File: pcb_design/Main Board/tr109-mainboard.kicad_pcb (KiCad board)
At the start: 2 copper layers, 60.3 x 60.4 mm, 30 parts, among them J1 Raspberry Pi Zero W, J2 ST7735_Screen, J3 Conn_01x04_Female, J4 Conn_01x09_Female, J5 Conn_01x03_Female, J6 Conn_01x02_Female, J6 Conn_01x02_Female-Connector, J7 Conn_01x03_Female, Q1 2N2222A, U1 CAP1206-x-SL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

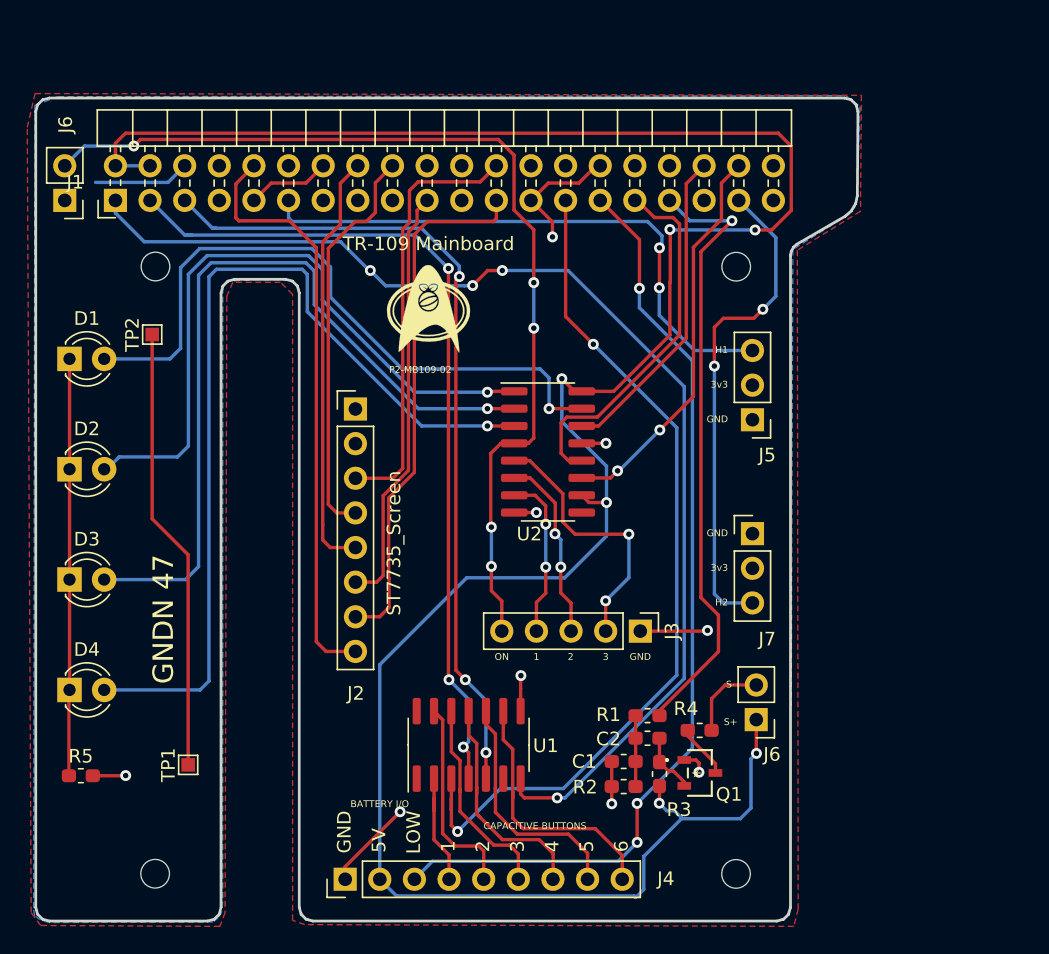
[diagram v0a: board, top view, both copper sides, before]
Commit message: cleanup and revisions
changes to the sensor and main boards
clean up of the blender file to remove some deprecated meshes
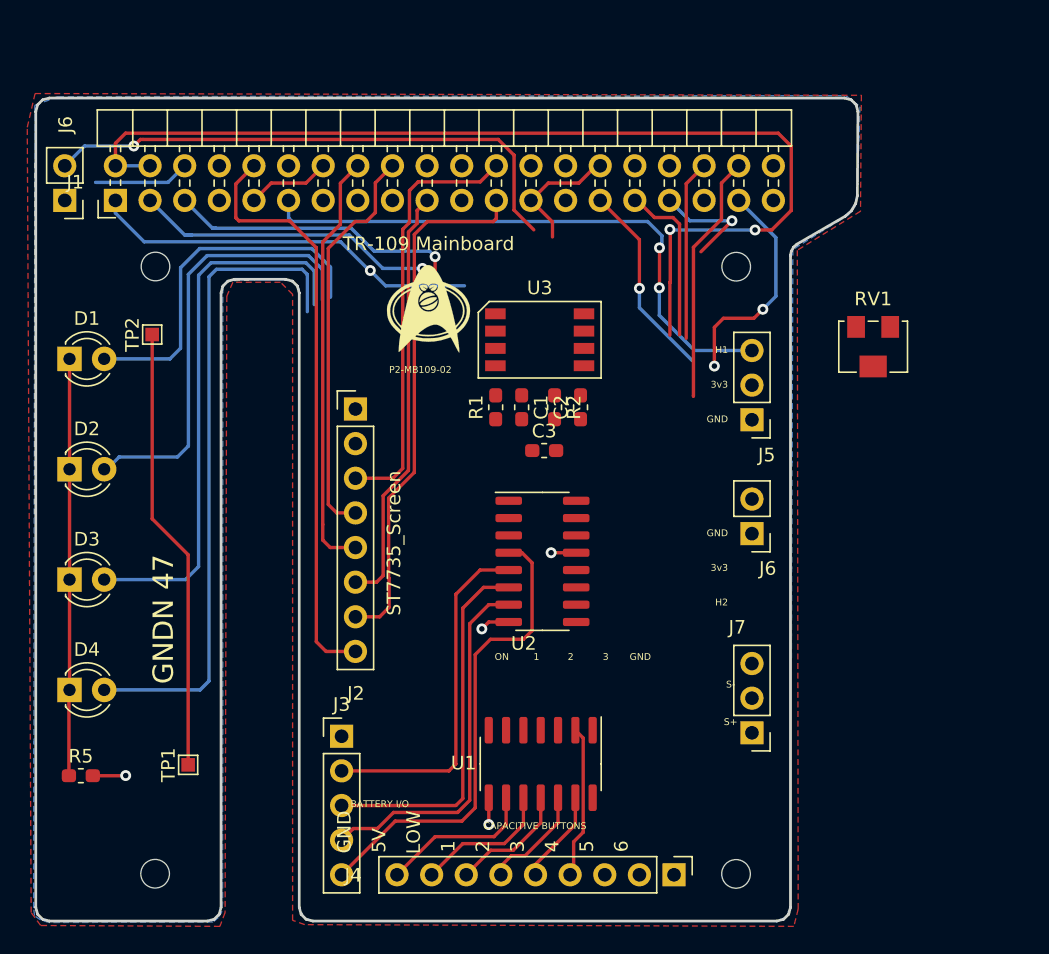
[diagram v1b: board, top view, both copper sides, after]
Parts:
- removed Q1: 2N2222A, footprints:SSTA06HZGT116
- removed R3: 15k, Resistor_SMD:R_0603_1608Metric_Pad1.05x0.95mm_HandSolder
- removed R4: 8, Resistor_SMD:R_0603_1608Metric_Pad1.05x0.95mm_HandSolder
- added C3: 10uF, Capacitor_SMD:C_0603_1608Metric_Pad1.05x0.95mm_HandSolder, F.Cu at (150.9, 96.9)
- added RV1: 10K, Potentiometer_SMD:Potentiometer_Bourns_3214W_Vertical, F.Cu at (175.0, 89.3)
- added U3: PAM8302AAS, Main Board:SOIC-8, F.Cu at (150.5, 88.8)
- C1: value C -> 1uF
- C2: value CP -> 1uF
- R1: value 270 -> 100
- R2: value 150 -> 100
- moved R2 28.3 mm to (151.6, 93.8), turned to 270 degrees
- moved C1 27.0 mm to (149.2, 93.8), turned to 270 degrees
- moved R1 25.2 mm to (147.3, 93.8), turned to 90 degrees
- moved C2 24.8 mm to (153.5, 93.8), turned to 90 degrees
- moved J4 24.1 mm to (160.4, 128.0), turned to 270 degrees
- moved J3 23.2 mm to (136.0, 117.9), turned to 0 degrees
- moved J7 14.6 mm to (166.1, 117.6), turned to 180 degrees
- moved J6 13.6 mm to (166.1, 103.0)
- moved U2 8.04 mm to (150.7, 105.1)
- moved U1 5.47 mm to (150.6, 119.9), turned to 270 degrees
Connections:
- C1 pad 2: GND -> Net-(C1-Pad2)
- C2 pad 1: Net-(C1-Pad1) -> Net-(C2-Pad1)
- C2 pad 2: Net-(C2-Pad2) -> GND
- R1 pad 1: AUDIO -> Net-(R1-Pad1)
- R2 pad 1: GND -> Net-(R2-Pad1)
- R2 pad 2: Net-(C1-Pad1) -> Net-(C2-Pad1)
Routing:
- net 5V: track 179.7 -> 76.5 mm, vias 6 -> 2
- net ALERT: track 63.9 -> 0.00 mm, vias 2 -> 0
- net 3v3: track 87.2 -> 28.7 mm, vias 4 -> 1
- net Bat_GPIO: track 69.0 -> 14.6 mm, vias 3 -> 1
- net SDA: track 62.9 -> 22.5 mm, vias 3 -> 1
- net SCL: track 60.9 -> 22.1 mm, vias 3 -> 1
- net AUDIO: track 44.8 -> 8.41 mm
- net LED1: track 49.1 -> 26.0 mm, vias 1 -> 0
- net Hall_Effect_Sensor2: track 36.2 -> 16.5 mm
- net LED4: track 66.6 -> 47.9 mm, vias 1 -> 0
- net LED3: track 58.1 -> 40.3 mm, vias 1 -> 0
- net LED2: track 49.2 -> 32.3 mm, vias 1 -> 0
- net GND: track 47.8 -> 31.0 mm, vias 9 -> 4
- net Shift_Latch: track 27.5 -> 12.1 mm
- net LED7: track 12.1 -> 27.0 mm, vias 2 -> 0
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
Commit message: Pcb and shell design work
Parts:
- removed G***: LOGO, logo2:smalldelta
- removed G***: LOGO, logo2:delta 3
- removed the J6 at (166.1, 103.0)
- removed the J6 at (115.7, 78.6)
- added J6: Conn_01x02_Female-Connector, Connector_PinHeader_2.54mm:PinHeader_1x02_P2.54mm_Vertical, F.Cu at (164.9, 103.0)
- J4: footprint Connector_PinHeader_2.54mm:PinHeader_1x09_P2.54mm_Vertical -> Connector_PinHeader_2.54mm:PinHeader_1x11_P2.54mm_Vertical
- U1: value CAP1206-x-SL -> CAP1208
- moved J7 43.6 mm to (122.9, 123.5), turned to 270 degrees
- moved J3 29.4 mm to (164.9, 112.0)
- moved RV1 26.0 mm to (150.5, 98.1)
- moved U2 15.2 mm to (150.6, 89.8)
- moved R1 15.2 mm to (146.5, 108.9), turned to 270 degrees
- moved C2 15.2 mm to (154.1, 108.9)
- moved C3 15.1 mm to (150.6, 112.1)
- moved U3 15.1 mm to (150.3, 103.9), turned to 90 degrees
- moved C1 15.1 mm to (149.0, 108.9), turned to 90 degrees
- moved R2 15.1 mm to (151.6, 108.9)
- moved R5 1.73 mm to (116.9, 119.0)
- moved J5 1.24 mm to (164.9, 94.7)
- moved J4 0.48 mm to (160.7, 128.4)
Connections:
- net Net-(J1-Pad35) renamed Shift_Serial_Sensor_Board
- net Net-(J1-Pad40) renamed Shift_Latch_Sensor_Board
- J1 pad 11: Hall_Effect_Sensor -> Net-(J1-Pad11)
- J1 pad 32: Net-(J1-Pad32) -> Hall_Effect_Sensor
- J1 pad 37: Hall_Effect_Sensor2 -> Shift_Clock_Sensor_Board
- J1 pad 7: Net-(J1-Pad7) -> Hall_Effect_Sensor2
- U1 pad 1: (no net) -> Cap_2
- U1 pad 10: Cap_5 -> Cap_7
- U1 pad 11: Cap_4 -> Cap_6
- U1 pad 12: Cap_3 -> Cap_5
- U1 pad 13: Cap_2 -> Cap_4
- U1 pad 14: (no net) -> Cap_3
- U1 pad 9: Cap_6 -> Cap_8
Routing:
- net 5V: track 76.5 -> 183.3 mm, vias 2 -> 8
- net 3v3: track 28.7 -> 98.5 mm, vias 1 -> 7
- net SDA: track 22.5 -> 72.9 mm, vias 1 -> 3
- net ALERT: track 0.00 -> 47.0 mm, vias 0 -> 4
- net SCL: track 22.1 -> 67.2 mm, vias 1 -> 3
- net Bat_GPIO: track 14.6 -> 51.9 mm, vias 1 -> 0
- net Hall_Effect_Sensor2: track 16.5 -> 52.2 mm, vias 2 -> 0
- net LED5: track 25.6 -> 53.4 mm, vias 0 -> 4
- net LED7: track 27.0 -> 53.3 mm, vias 0 -> 4
- net LED6: track 27.1 -> 53.2 mm, vias 0 -> 3
- net Hall_Effect_Sensor: track 43.0 -> 20.1 mm, vias 2 -> 1
- net Net-(J6-Pad2): track 0.00 -> 22.2 mm, vias 0 -> 1
- net LED1: track 26.0 -> 45.2 mm, vias 0 -> 1
- net LED4: track 47.9 -> 67.0 mm, vias 0 -> 1
- net Net-(J6-Pad1): track 0.00 -> 18.2 mm, vias 0 -> 1
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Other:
- board text added: "7"
- board text added: "8"
- board text added: "P2-MB109-03"
- board text removed: "P2-MB109-02"

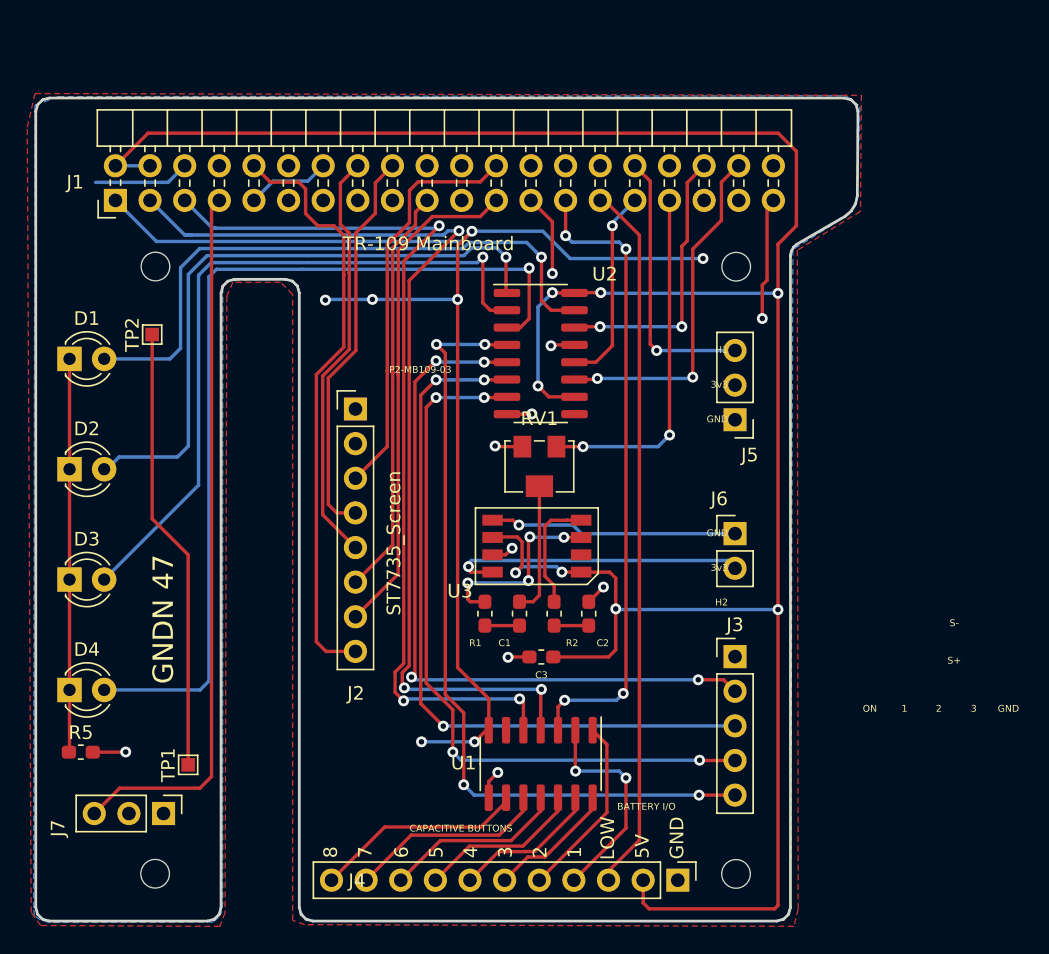
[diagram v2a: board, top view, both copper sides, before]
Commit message: Rev 3 board changes, blender file changes
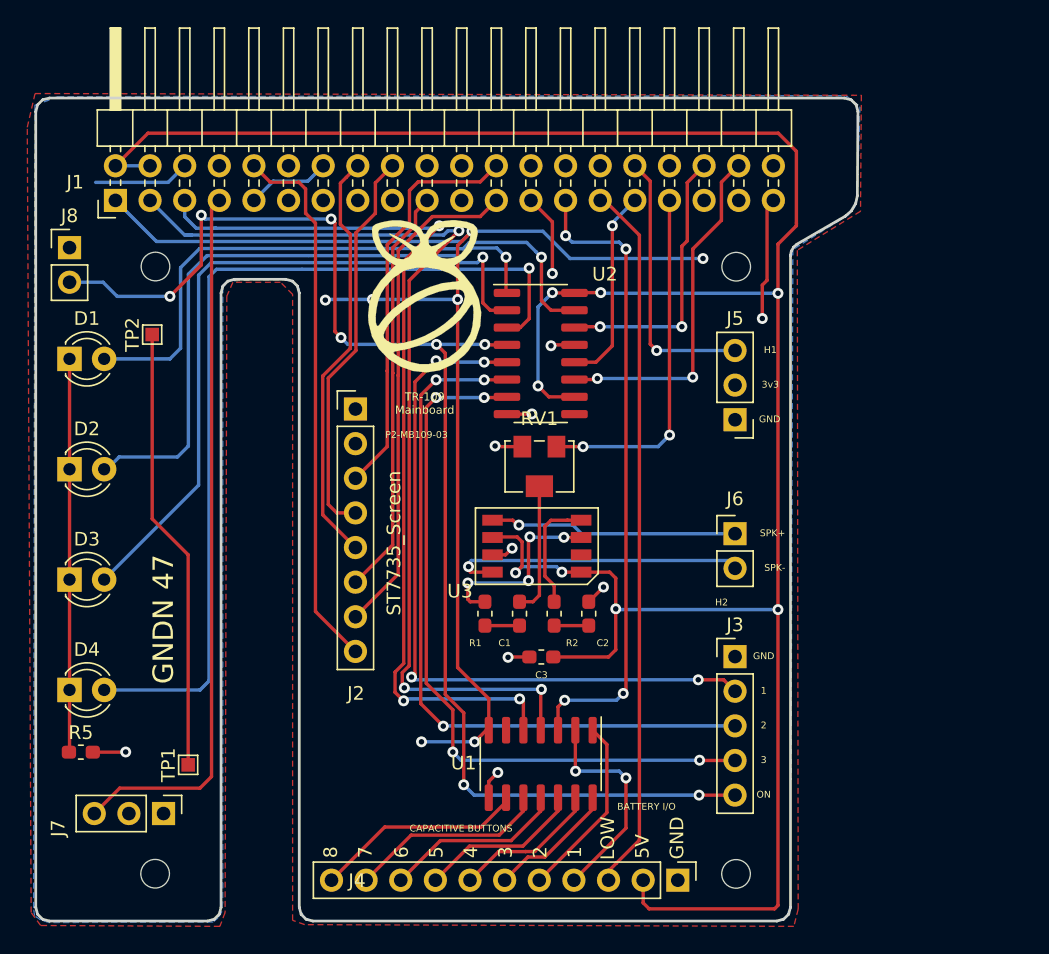
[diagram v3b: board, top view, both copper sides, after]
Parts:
- added G***: Picorder Logo, Logos:Untitled, F.Cu at (142.1, 85.5)
- added G***: Picorder Logo, Logos:Untitled, B.Cu at (150.9, 101.8)
- added J8: Led_On, Connector_PinHeader_2.54mm:PinHeader_1x02_P2.54mm_Vertical, F.Cu at (116.0, 82.0)
- J3: value Conn_01x04_Female -> Light_Board
- J4: value Conn_01x09_Female -> Cap_and_Bat
- J5: value Conn_01x03_Female -> Hall_1
- J7: value Conn_01x03_Female -> Hall_2
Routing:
- net LED_ON: track 58.5 -> 99.1 mm, vias 4 -> 8
- net SC_LED: track 43.6 -> 39.9 mm
- net SCL: track 67.2 -> 67.9 mm
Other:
- rule pad_to_mask_clearance: 0.0508 -> 0
- board text added: "Caution: Continued operation known to cause Delta Radiation Poisoning on Betazed"
- board text added: "P2-MB109-03 - Skurf Duotronics - 2021"
- board text added: "SPK+"
- board text added: "SPK-"
- board text added: "TR 109 - Mainboard"
- board text removed: "Caution: Known to cause Delta Radiation Poisoning on Betazed"
- board text removed: "P2-MB109-02 - Skurf Duotronics - CB 2021"
- board text removed: "Picorder 2 - TR 109"
- board text removed: "S+"
- board text removed: "S-"

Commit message: changes to shell and pcb
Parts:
- added J10: raw_audio_out, Connector_PinHeader_2.54mm:PinHeader_1x01_P2.54mm_Vertical, F.Cu at (164.9, 99.3)
- added J9: i2c_bus, Connector_PinHeader_2.54mm:PinHeader_1x02_P2.54mm_Vertical, F.Cu at (135.3, 119.7)
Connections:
- net Net-(J1-Pad11) renamed BUT1
- net Net-(J1-Pad13) renamed BUT2
- net Net-(J1-Pad15) renamed BUT3
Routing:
- net SDA: track 72.9 -> 86.3 mm, vias 3 -> 4
- net SCL: track 67.9 -> 76.9 mm, vias 3 -> 4
- net AUDIO: track 25.9 -> 33.0 mm
- net LED7: vias 4 -> 3
- net LED_ON: vias 8 -> 7
- net LED5: vias 4 -> 3
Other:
- board text added: "HES-2"
- board text removed: "H2"

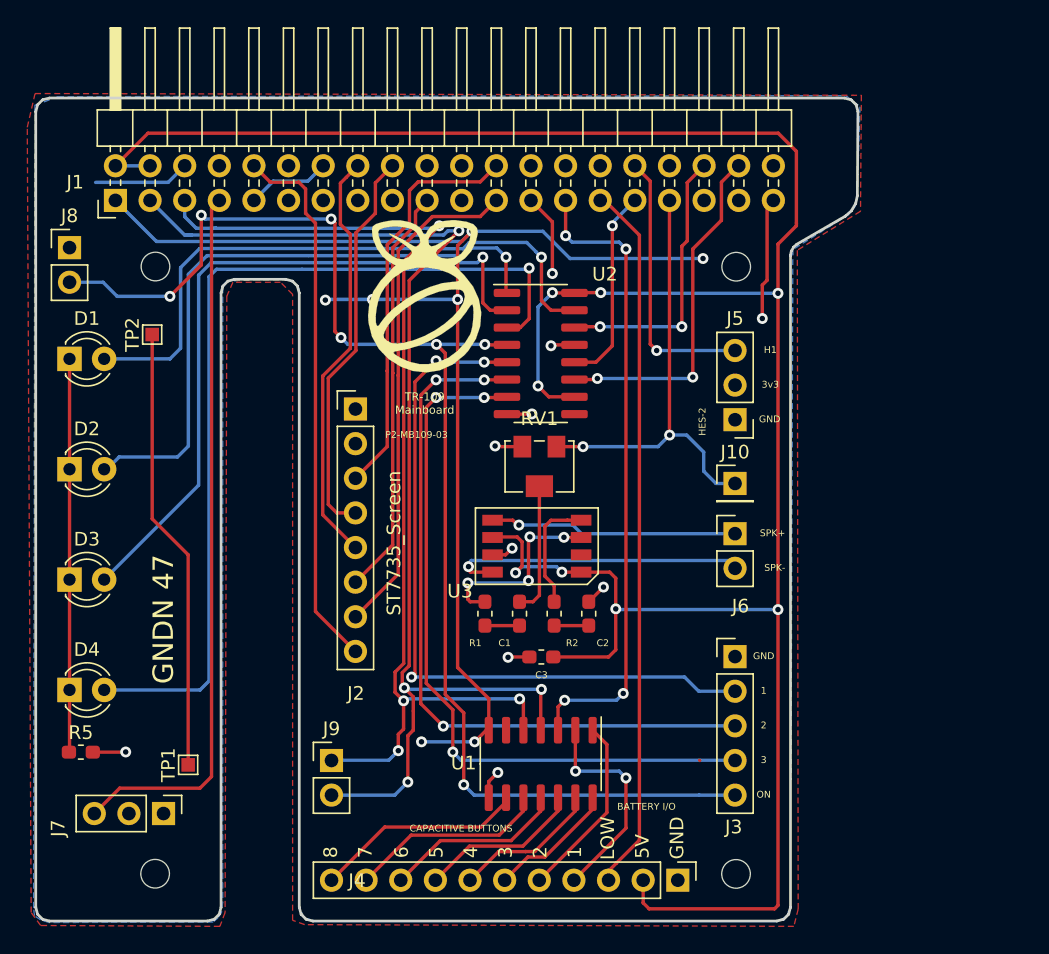
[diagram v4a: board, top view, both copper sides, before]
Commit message: Kicad V8 updates
Changes to board and improvements. Needs Kicad V8 now.
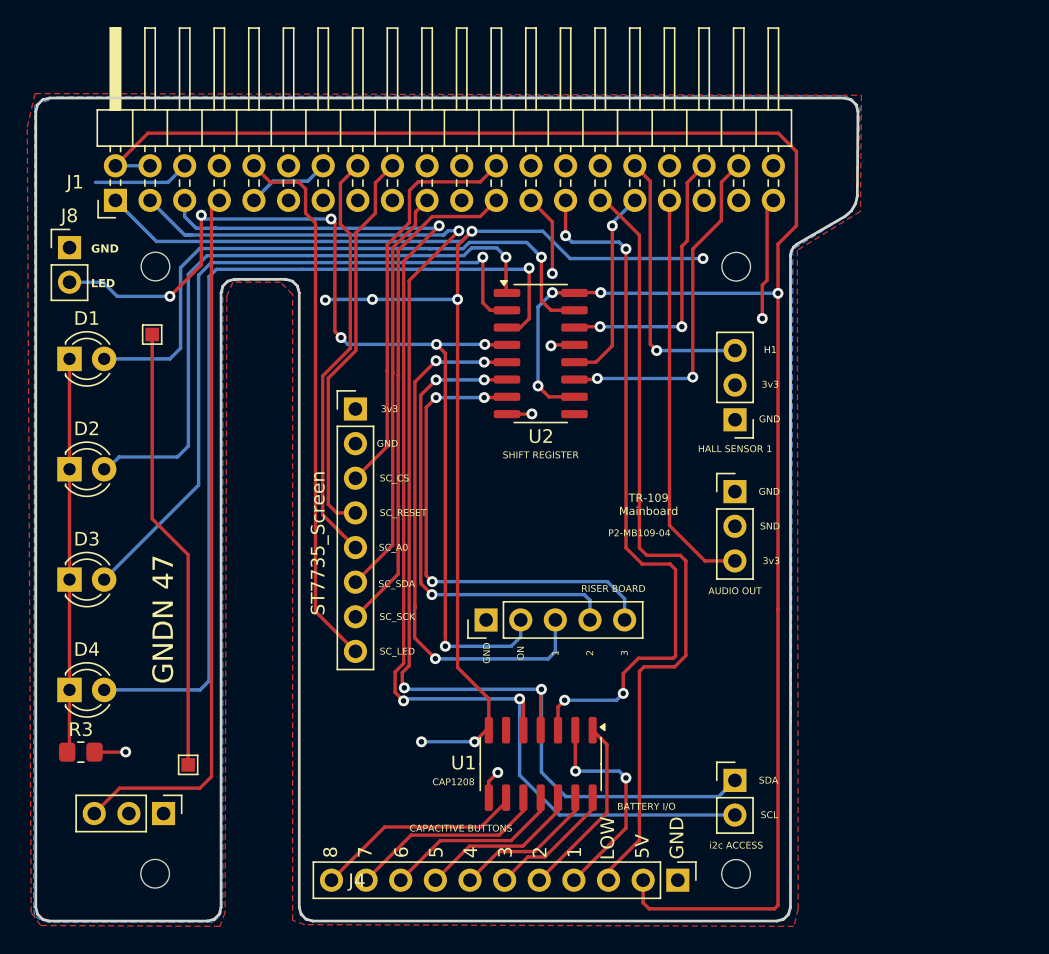
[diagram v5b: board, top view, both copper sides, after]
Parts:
- removed C1, C2: 1uF, Capacitor_SMD:C_0603_1608Metric_Pad1.05x0.95mm_HandSolder
- removed C3: 10uF, Capacitor_SMD:C_0603_1608Metric_Pad1.05x0.95mm_HandSolder
- removed the G*** at (142.1, 85.5)
- removed the G*** at (150.9, 101.8)
- removed J10: raw_audio_out, Connector_PinHeader_2.54mm:PinHeader_1x01_P2.54mm_Vertical
- removed R1, R2: 100, Resistor_SMD:R_0603_1608Metric_Pad1.05x0.95mm_HandSolder
- removed RV1: 10K, Potentiometer_SMD:Potentiometer_Bourns_3214W_Vertical
- removed U3: PAM8302AAS, Main Board:SOIC-8
- added G***: Picorder Logo, Logos:Picorder Logo, B.Cu at (150.9, 101.0)
- D1, D2, D3, D4: value LED -> Green_LED
- J6: value Conn_01x02_Female-Connector -> Audio_Out; footprint Connector_PinHeader_2.54mm:PinHeader_1x02_P2.54mm_Vertical -> Connector_PinHeader_2.54mm:PinHeader_1x03_P2.54mm_Vertical
- J9: value i2c_bus -> i2c Connect
- R3: renamed from R5; footprint Resistor_SMD:R_0603_1608Metric_Pad1.05x0.95mm_HandSolder -> Resistor_SMD:R_0805_2012Metric_Pad1.20x1.40mm_HandSolder
- moved J9 29.6 mm to (164.8, 121.1)
- moved J3 18.5 mm to (146.6, 109.3), turned to 90 degrees
- moved J6 3.08 mm to (164.8, 99.9)
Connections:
- net Net-(J1-Pad12) renamed PG_NS
- net Net-(J1-Pad22) renamed PG_SIG
- J1 pad 17: Net-(J1-Pad17) -> unconnected-(J1-3V3-Pad17)
- J1 pad 21: Net-(J1-Pad21) -> unconnected-(J1-MISO0/GPIO9-Pad21)
- J1 pad 26: Net-(J1-Pad26) -> unconnected-(J1-~{CE1}/GPIO7-Pad26)
- J1 pad 28: Net-(J1-Pad28) -> unconnected-(J1-ID_SC/GPIO1-Pad28)
- J1 pad 8: Net-(J1-Pad8) -> unconnected-(J1-GPIO14/TXD-Pad8)
- J3 pad 2: LED5 -> LED_ON
- J3 pad 3: LED6 -> LED5
- J3 pad 4: LED7 -> LED6
- J3 pad 5: LED_ON -> LED7
- J6 pad 1: Net-(J6-Pad1) -> GND
- J6 pad 2: Net-(J6-Pad2) -> 3v3
- J9 pad 1: SCL -> SDA
- J9 pad 2: SDA -> SCL
- U2 pad 9: Net-(U2-Pad9) -> unconnected-(U2-QH'-Pad9)
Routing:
- net 5V: track 183.3 -> 148.6 mm, vias 8 -> 4
- net LED_ON: track 99.1 -> 75.2 mm
- net Net-(J6-Pad2): track 22.2 -> 0.00 mm, vias 1 -> 0
- net Net-(J6-Pad1): track 18.2 -> 0.00 mm, vias 1 -> 0
- net LED6: track 53.2 -> 35.0 mm
- net LED7: track 53.3 -> 35.4 mm
- net Net-(R1-Pad1): track 14.1 -> 0.00 mm, vias 4 -> 0
- net SCL: track 76.9 -> 90.5 mm, vias 4 -> 3
- net LED5: track 53.4 -> 39.9 mm
- net Net-(C1-Pad2): track 9.66 -> 0.00 mm
- net Net-(R2-Pad1): track 8.66 -> 0.00 mm
- net SDA: track 86.3 -> 94.4 mm, vias 4 -> 3
- net GND: track 43.4 -> 36.6 mm, vias 10 -> 6
- net ALERT: track 47.0 -> 52.7 mm
- net Bat_GPIO: track 51.9 -> 57.5 mm
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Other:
- net class Default removed
- board text added: "AUDIO OUT"
- board text added: "CAP1208"
- board text added: "HALL SENSOR 1"
- board text added: "LED"
- board text added: "P2-MB109-04"
- board text added: "P2-MB109-04 - Skurf Isolinear - 2024"
- board text added: "RISER BOARD"
- board text added: "SCL"
- board text added: "SC_A0"
- board text added: "SC_CS"
- board text added: "SC_LED"
- board text added: "SC_RESET"
- board text added: "SC_SCK"
- board text added: "SC_SDA"
- board text added: "SDA"
- board text added: "SHIFT REGISTER"
- board text added: "SND"
- board text added: "i2c ACCESS"
- board text removed: "HES-2"
- board text removed: "P2-MB109-03"
- board text removed: "P2-MB109-03 - Skurf Duotronics - 2021"
- board text removed: "SPK+"
- board text removed: "SPK-"
